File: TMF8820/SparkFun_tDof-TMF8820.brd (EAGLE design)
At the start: 25.4 x 25.4 mm, 22 parts, among them J4 QWIIC_RIGHT_ANGLE, J5 QWIIC_RIGHT_ANGLE

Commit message: Adds an additional folder for second part
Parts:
- renumbered JP2 to LED, JP4 to I2C
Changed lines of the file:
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@@
 <attribute name="VALUE" x="35.4838" y="44.3484" size="0.6096" layer="27" font="vector" ratio="20" align="top-center"/>
 </element>
-<element name="JP2" library="SparkFun-Jumpers" package="SMT-JUMPER_2_NC_TRACE_SILK" package3d_urn="urn:adsk.eagle:package:39281/1" value="LED" x="35.56" y="43.18" smashed="yes" rot="MR0">
+<element name="LED" library="SparkFun-Jumpers" package="SMT-JUMPER_2_NC_TRACE_SILK" package3d_urn="urn:adsk.eagle:package:39281/1" value="LED" x="35.56" y="43.18" smashed="yes" rot="MR0">
 <attribute name="NAME" x="35.56" y="44.323" size="0.6096" layer="26" font="vector" ratio="20" rot="MR0" align="bottom-center"/>
 <attribute name="VALUE" x="35.56" y="42.037" size="0.6096" layer="28" font="vector" ratio="20" rot="MR0" align="top-center"/>
 </element>
-<element name="JP4" library="SparkFun-Jumpers" package="SMT-JUMPER_3_2-NC_TRACE_SILK" package3d_urn="urn:adsk.eagle:package:39289/1" value="I2C_PU" x="55.88" y="43.18" smashed="yes" rot="MR0">
+<element name="I2C" library="SparkFun-Jumpers" package="SMT-JUMPER_3_2-NC_TRACE_SILK" package3d_urn="urn:adsk.eagle:package:39289/1" value="I2C_PU" x="55.88" y="43.18" smashed="yes" rot="MR0">
 <attribute name="NAME" x="55.88" y="44.323" size="0.6096" layer="26" font="vector" ratio="20" rot="MR0" align="bottom-center"/>
 <attribute name="VALUE" x="55.88" y="42.037" size="0.6096" layer="28" font="vector" ratio="20" rot="MR0" align="top-center"/>
@@
 <contactref element="J5" pad="2"/>
 <contactref element="J6" pad="2"/>
-<contactref element="JP2" pad="2"/>
-<contactref element="JP4" pad="2"/>
+<contactref element="LED" pad="2"/>
+<contactref element="I2C" pad="2"/>
 <wire x1="55.88" y1="43.18" x2="55.88" y2="38.862" width="0.254" layer="16"/>
 <via x="55.88" y="38.862" extent="1-16" drill="0.381"/>
@@
 <signal name="N$6">
 <contactref element="R6" pad="2"/>
-<contactref element="JP2" pad="1"/>
+<contactref element="LED" pad="1"/>
 <wire x1="36.0807" y1="43.18" x2="37.846" y2="43.18" width="0.254" layer="16"/>
 <via x="37.846" y="43.18" extent="1-16" drill="0.381"/>
@@
 <signal name="N$7">
 <contactref element="R3" pad="2"/>
-<contactref element="JP4" pad="3"/>
+<contactref element="I2C" pad="3"/>
 <via x="54.229" y="46.7106" extent="1-16" drill="0.381"/>
 <wire x1="54.229" y1="46.7106" x2="54.864" y2="46.0756" width="0.254" layer="16"/>
@@
 </signal>
 <signal name="N$8">
-<contactref element="JP4" pad="1"/>
+<contactref element="I2C" pad="1"/>
 <contactref element="R5" pad="2"/>
 <via x="57.658" y="46.7106" extent="1-16" drill="0.381"/>

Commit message: Moves correct TMF8820 files into the correct folder
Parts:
- added C1, C2, C3: 0.1uF, SparkFun-Capacitors:0402-TIGHT
- added J1: (no value), SparkFun-Connectors:1X04_NO_SILK
- added R1, R2: 10k, SparkFun-Resistors:0603
- added U$1: TMF8820-, TMF882X:TMF882X
- added U$10: (no value), TMFTopSilk:##INT##8
- added U$11: (no value), TMFTopSilk:TMF88209
- added U$12: (no value), TMFTopSilk:DTOF882188211
- added U$13: (no value), SparkFun-Aesthetics:SFE_LOGO_NAME_.1
- added U$14: (no value), TMFTopSilk:PWR882188212
- added U$15: (no value), TMFBotSilk:##INT##9
- added U$16: (no value), TMFBotSilk:#3V3#0
- added U$17: (no value), TMFBotSilk:#EN#7
- added U$18: (no value), TMFBotSilk:#GND#4
- added U$19: (no value), TMFBotSilk:#GPIO1#8
- added U$2: (no value), TMFTopSilk:#3V3#0
- added U$20: (no value), TMFBotSilk:#I2C#11
- added U$21: (no value), TMFBotSilk:#SCL#5
- added U$22: (no value), TMFBotSilk:#LED#10
- added U$23: (no value), TMFBotSilk:#SDA#6
- added U$24: (no value), TMFBotSilk:#SYNC#8
- added U$26: (no value), TMFTopSilk:TMF882021
- added U$27: (no value), TMFTopSilk:DTOF8821882023
- added U$28: (no value), TMFBotSilk:DEF11
- added U$29: (no value), TMFBotSilk:ADDR#12
- added U$3: (no value), TMFTopSilk:#GND#4
- added U$30: (no value), TMFBotSilk:0X4113
- added U$4: (no value), TMFTopSilk:#SDA#6
- added U$5: (no value), TMFTopSilk:#SCL#5
- added U$7: (no value), TMFTopSilk:#EN#7
- added U$8: (no value), TMFTopSilk:GPIO18
- added U$9: (no value), TMFTopSilk:GPIO019
- moved LOGO4 15.6 mm to (35.3, 32.6)
- moved R3 14.8 mm to (44.3, 34.3)
- moved R5 14.6 mm to (46.9, 34.3)
- moved I2C 13.5 mm to (45.7, 34.3)
- moved LOGO3 6.22 mm to (45.7, 40.8)
- moved R6 1.39 mm to (35.9, 45.0), turned to 270 degrees
- moved D2 1.04 mm to (34.4, 45.0), turned to 270 degrees
- moved U$25 0.57 mm to (56.6, 34.3), turned to 90 degrees
- moved U$6 0.36 mm to (35.6, 35.1)
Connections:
- new net !INT!: J1.4, R1.1, U$1.P4
- new net EN: J1.1, R2.1, U$1.P9
- new net GPIO0/SYNC: J1.3, U$1.P3
- new net GPIO1: J1.2, U$1.P10
- net 3.3V: now also C1.1, C2.1, C3.1, R1.2, R2.2, U$1.P1, U$1.P12, U$1.P7
- net GND: now also C1.2, C2.2, C3.2, U$1.P11, U$1.P2, U$1.P8
- net SCL: now also U$1.P5
- net SDA: now also U$1.P6
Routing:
- net 3.3V: track 6.86 -> 60.3 mm, vias 1 -> 8
- net SDA: track 5.35 -> 38.7 mm, vias 2 -> 1
- net SCL: track 5.72 -> 38.2 mm
- net EN: track 0.00 -> 22.8 mm, vias 0 -> 3
- net !INT!: track 0.00 -> 21.1 mm, vias 0 -> 2
- net GPIO0/SYNC: track 0.00 -> 17.1 mm
- net GPIO1: track 0.00 -> 16.4 mm, vias 0 -> 1
- net GND: track 0.00 -> 3.73 mm, vias 0 -> 23
- net N$8: track 5.18 -> 2.66 mm
- net N$7: track 5.21 -> 2.74 mm
- net N$6: track 3.36 -> 2.82 mm

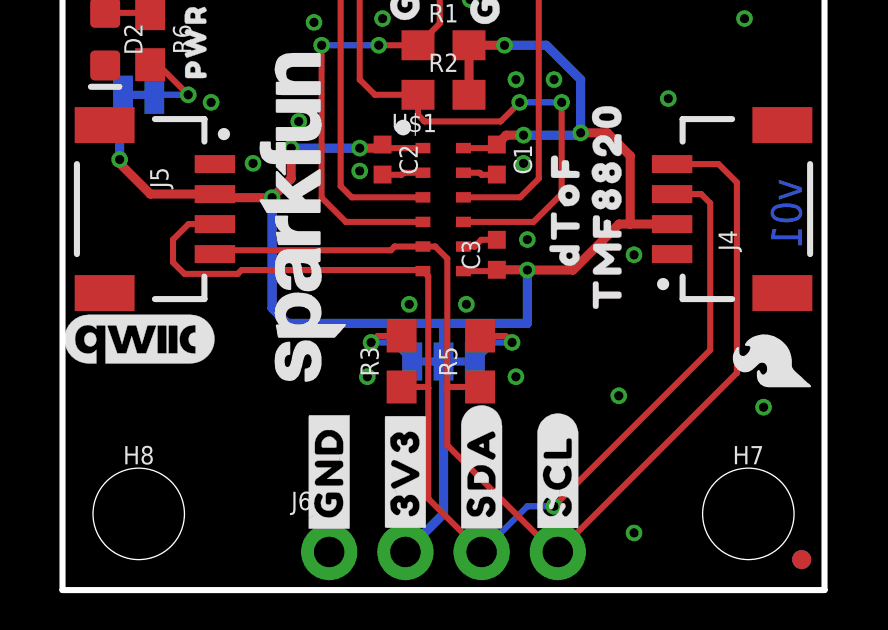
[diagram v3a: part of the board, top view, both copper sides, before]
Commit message: Adds default address to HQ boards, fixes some clearance issues
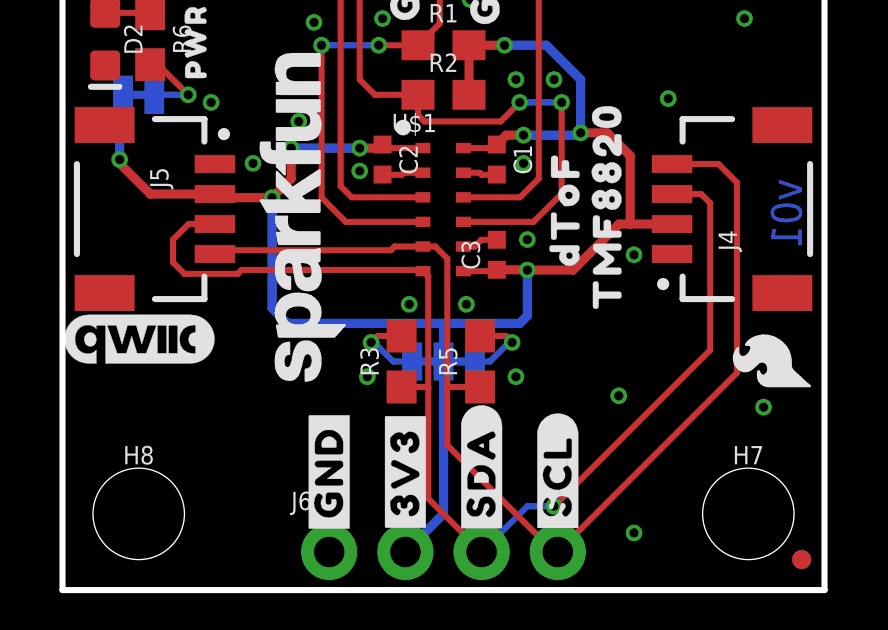
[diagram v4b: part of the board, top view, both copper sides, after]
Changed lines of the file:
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@@
 <layer number="19" name="Unrouted" color="6" fill="1" visible="yes" active="yes"/>
 <layer number="20" name="Dimension" color="15" fill="1" visible="yes" active="yes"/>
-<layer number="21" name="tPlace" color="16" fill="1" visible="yes" active="yes"/>
-<layer number="22" name="bPlace" color="14" fill="1" visible="yes" active="yes"/>
+<layer number="21" name="tPlace" color="16" fill="1" visible="no" active="yes"/>
+<layer number="22" name="bPlace" color="14" fill="1" visible="no" active="yes"/>
 <layer number="23" name="tOrigins" color="15" fill="1" visible="yes" active="yes"/>
 <layer number="24" name="bOrigins" color="15" fill="1" visible="yes" active="yes"/>
@@
 <layer number="37" name="tTest" color="7" fill="1" visible="no" active="yes"/>
 <layer number="38" name="bTest" color="7" fill="1" visible="no" active="yes"/>
-<layer number="39" name="tKeepout" color="4" fill="11" visible="no" active="yes"/>
+<layer number="39" name="tKeepout" color="4" fill="11" visible="yes" active="yes"/>
 <layer number="40" name="bKeepout" color="1" fill="11" visible="no" active="yes"/>
 <layer number="41" name="tRestrict" color="4" fill="10" visible="no" active="yes"/>
@@
 <layer number="115" name="ReferenceISLANDS" color="7" fill="1" visible="no" active="no"/>
 <layer number="116" name="Patch_BOT" color="9" fill="4" visible="no" active="no"/>
-<layer number="117" name="PM_Ref" color="26" fill="1" visible="yes" active="yes"/>
+<layer number="117" name="PM_Ref" color="26" fill="1" visible="no" active="yes"/>
 <layer number="118" name="Rect_Pads" color="7" fill="1" visible="no" active="no"/>
-<layer number="119" name="PF_Ref" color="31" fill="1" visible="yes" active="yes"/>
-<layer number="120" name="WFL_Ref" color="25" fill="1" visible="yes" active="yes"/>
+<layer number="119" name="PF_Ref" color="31" fill="1" visible="no" active="yes"/>
+<layer number="120" name="WFL_Ref" color="25" fill="1" visible="no" active="yes"/>
 <layer number="121" name="_tsilk" color="7" fill="1" visible="no" active="no"/>
 <layer number="122" name="_bsilk" color="7" fill="1" visible="no" active="no"/>
@@
 <wire x1="45.72" y1="35.56" x2="40.513" y2="35.56" width="0.3048" layer="16"/>
 <wire x1="40.513" y1="35.56" x2="40.005" y2="36.068" width="0.3048" layer="16"/>
-<wire x1="45.72" y1="35.56" x2="48.514" y2="35.56" width="0.3048" layer="16"/>
-<wire x1="48.514" y1="35.56" x2="48.514" y2="37.338" width="0.3048" layer="16"/>
+<wire x1="45.72" y1="35.56" x2="48.26" y2="35.56" width="0.3048" layer="16"/>
 <wire x1="47.498" y1="37.346" x2="48.506" y2="37.346" width="0.3048" layer="1"/>
 <wire x1="48.506" y1="37.346" x2="48.514" y2="37.338" width="0.3048" layer="1"/>
+<wire x1="48.26" y1="35.56" x2="48.514" y2="35.814" width="0.3048" layer="16"/>
+<wire x1="48.514" y1="35.814" x2="48.514" y2="37.338" width="0.3048" layer="16"/>
 <wire x1="45.72" y1="34.289996875" x2="45.72" y2="34.29" width="0" layer="19" extent="16-16"/>
 </signal>
@@
 <contactref element="R3" pad="2"/>
 <contactref element="I2C" pad="3"/>
-<wire x1="44.6786" y1="34.29" x2="44.0436" y2="34.925" width="0.2032" layer="16"/>
-<wire x1="44.0436" y1="34.925" x2="43.307" y2="34.925" width="0.2032" layer="16"/>
+<wire x1="44.6786" y1="34.29" x2="44.0436" y2="34.29" width="0.2032" layer="16"/>
+<wire x1="44.0436" y1="34.29" x2="43.4086" y2="34.925" width="0.2032" layer="16"/>
+<wire x1="43.4086" y1="34.925" x2="43.307" y2="34.925" width="0.2032" layer="16"/>
 <via x="43.307" y="34.925" extent="1-16" drill="0.3048"/>
 <wire x1="44.323" y1="35.14" x2="43.522" y2="35.14" width="0.2032" layer="1"/>
@@
 <contactref element="I2C" pad="1"/>
 <contactref element="R5" pad="2"/>
-<wire x1="48.006" y1="34.925" x2="47.3964" y2="34.925" width="0.2032" layer="16"/>
-<wire x1="46.7614" y1="34.29" x2="47.3964" y2="34.925" width="0.2032" layer="16"/>
+<wire x1="48.006" y1="34.925" x2="47.9044" y2="34.925" width="0.2032" layer="16"/>
+<wire x1="47.9044" y1="34.925" x2="47.2694" y2="34.29" width="0.2032" layer="16"/>
+<wire x1="46.7614" y1="34.29" x2="47.2694" y2="34.29" width="0.2032" layer="16"/>
 <via x="48.006" y="34.925" extent="1-16" drill="0.3048"/>
 <wire x1="48.006" y1="34.925" x2="47.791" y2="35.14" width="0.2032" layer="1"/>

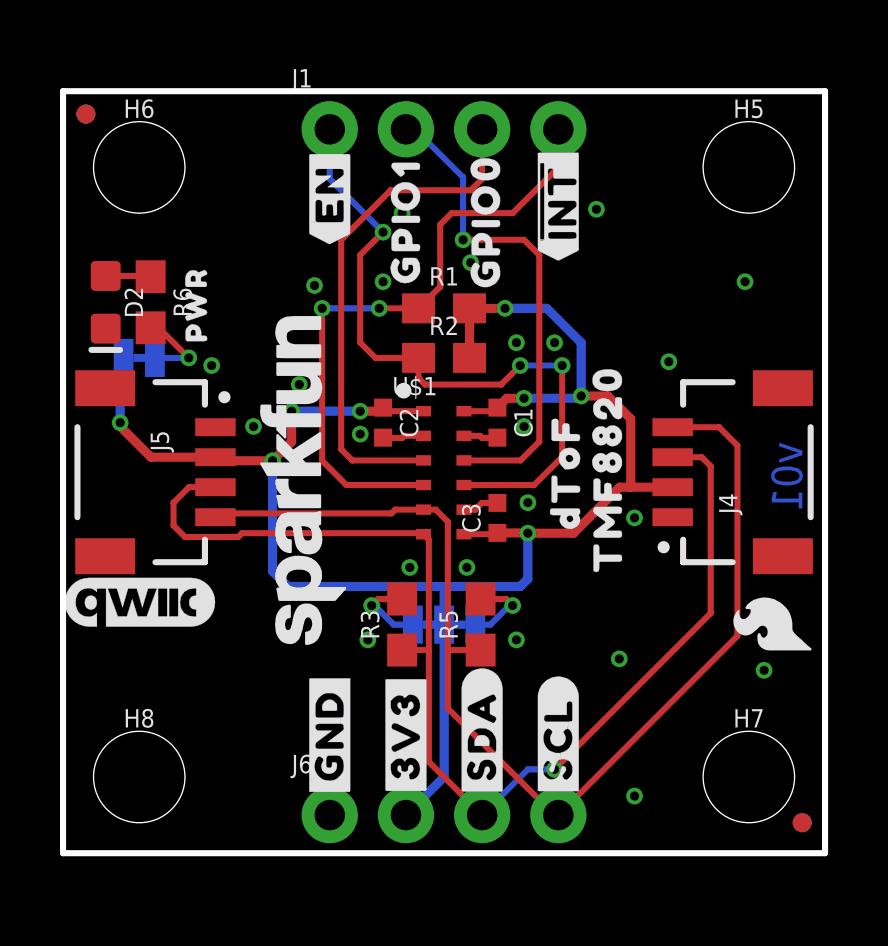
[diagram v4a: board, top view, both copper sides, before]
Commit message: Moves header to one side on the 1"x1" Qwiic Board
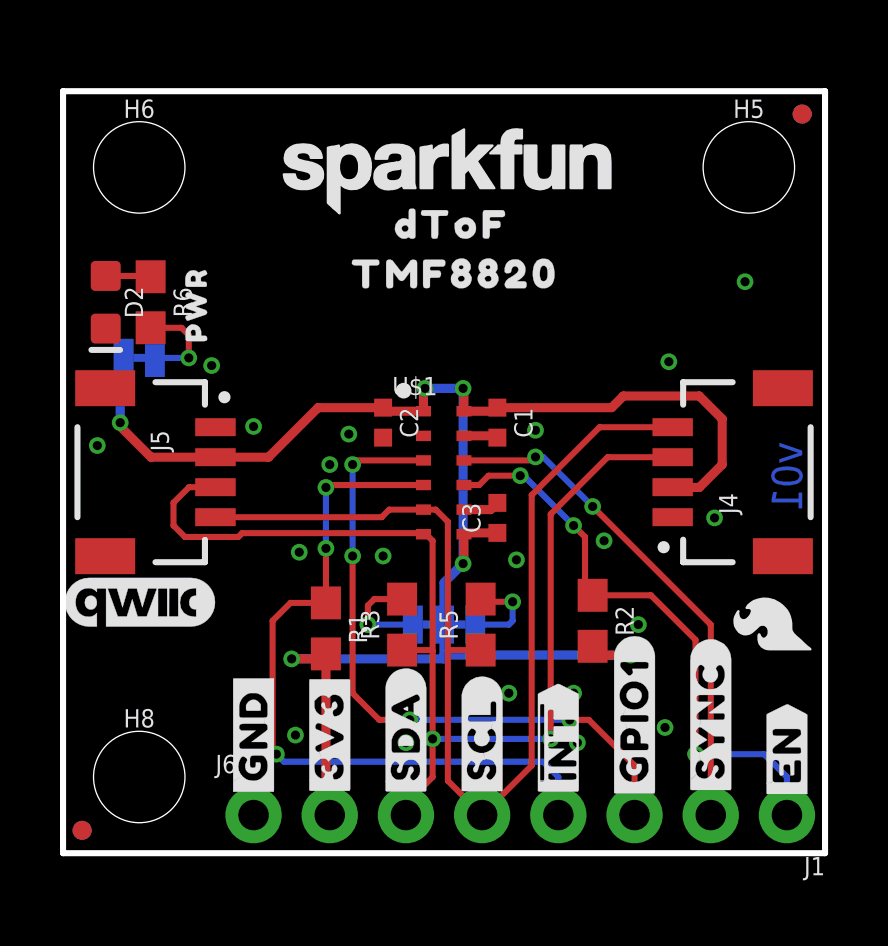
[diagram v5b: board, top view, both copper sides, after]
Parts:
- removed H7: STAND-OFFTIGHT, SparkFun-Hardware:STAND-OFF-TIGHT
- removed U$8: (no value), TMFTopSilk:GPIO18
- removed U$9: (no value), TMFTopSilk:GPIO019
- moved J1 27.5 mm to (57.1, 27.9), turned to 180 degrees
- moved U$17 24.1 mm to (57.1, 30.0), flipped to the top, turned to 90 degrees
- moved U$7 24.1 mm to (57.1, 30.0), flipped to the bottom, turned to 270 degrees
- moved FD5 24.0 mm to (33.7, 27.4)
- moved FD8 24.0 mm to (33.7, 27.4)
- moved FD6 23.9 mm to (57.7, 51.3)
- moved FD7 23.9 mm to (57.7, 51.3)
- moved U$24 18.2 mm to (54.6, 31.1), flipped to the top, turned to 90 degrees
- moved U$19 18.1 mm to (52.1, 31.1), flipped to the top, turned to 90 degrees
- moved U$10 18.0 mm to (49.5, 30.4), flipped to the bottom, turned to 270 degrees
- moved U$15 18.0 mm to (49.5, 30.4), flipped to the top, turned to 90 degrees
- moved R1 11.4 mm to (41.8, 34.2), turned to 270 degrees
- moved U$13 11.4 mm to (45.8, 49.4), turned to 0 degrees
- moved R2 10.1 mm to (50.7, 34.4), turned to 270 degrees
- moved U$12 9.09 mm to (46.0, 47.6), turned to 0 degrees
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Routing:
- net GPIO0/SYNC: track 17.1 -> 22.1 mm, vias 0 -> 4
- net !INT!: track 21.1 -> 24.6 mm, vias 2 -> 3
- net EN: track 22.8 -> 19.5 mm
- net SCL: track 38.2 -> 36.4 mm
- net GND: track 3.73 -> 2.35 mm, vias 23 -> 21
- net N$7: track 2.74 -> 3.37 mm
- net SDA: track 38.7 -> 38.1 mm, vias 1 -> 2
- net GPIO1: track 16.4 -> 16.9 mm, vias 1 -> 2
- net 3.3V: track 60.2 -> 59.8 mm, vias 8 -> 6
